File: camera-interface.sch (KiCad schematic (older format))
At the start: 44 parts, among them J8 WE_68715014522, U19 NTS0102GT, U20 NTS0102GT, U22 AP2114H-3_3TRG1

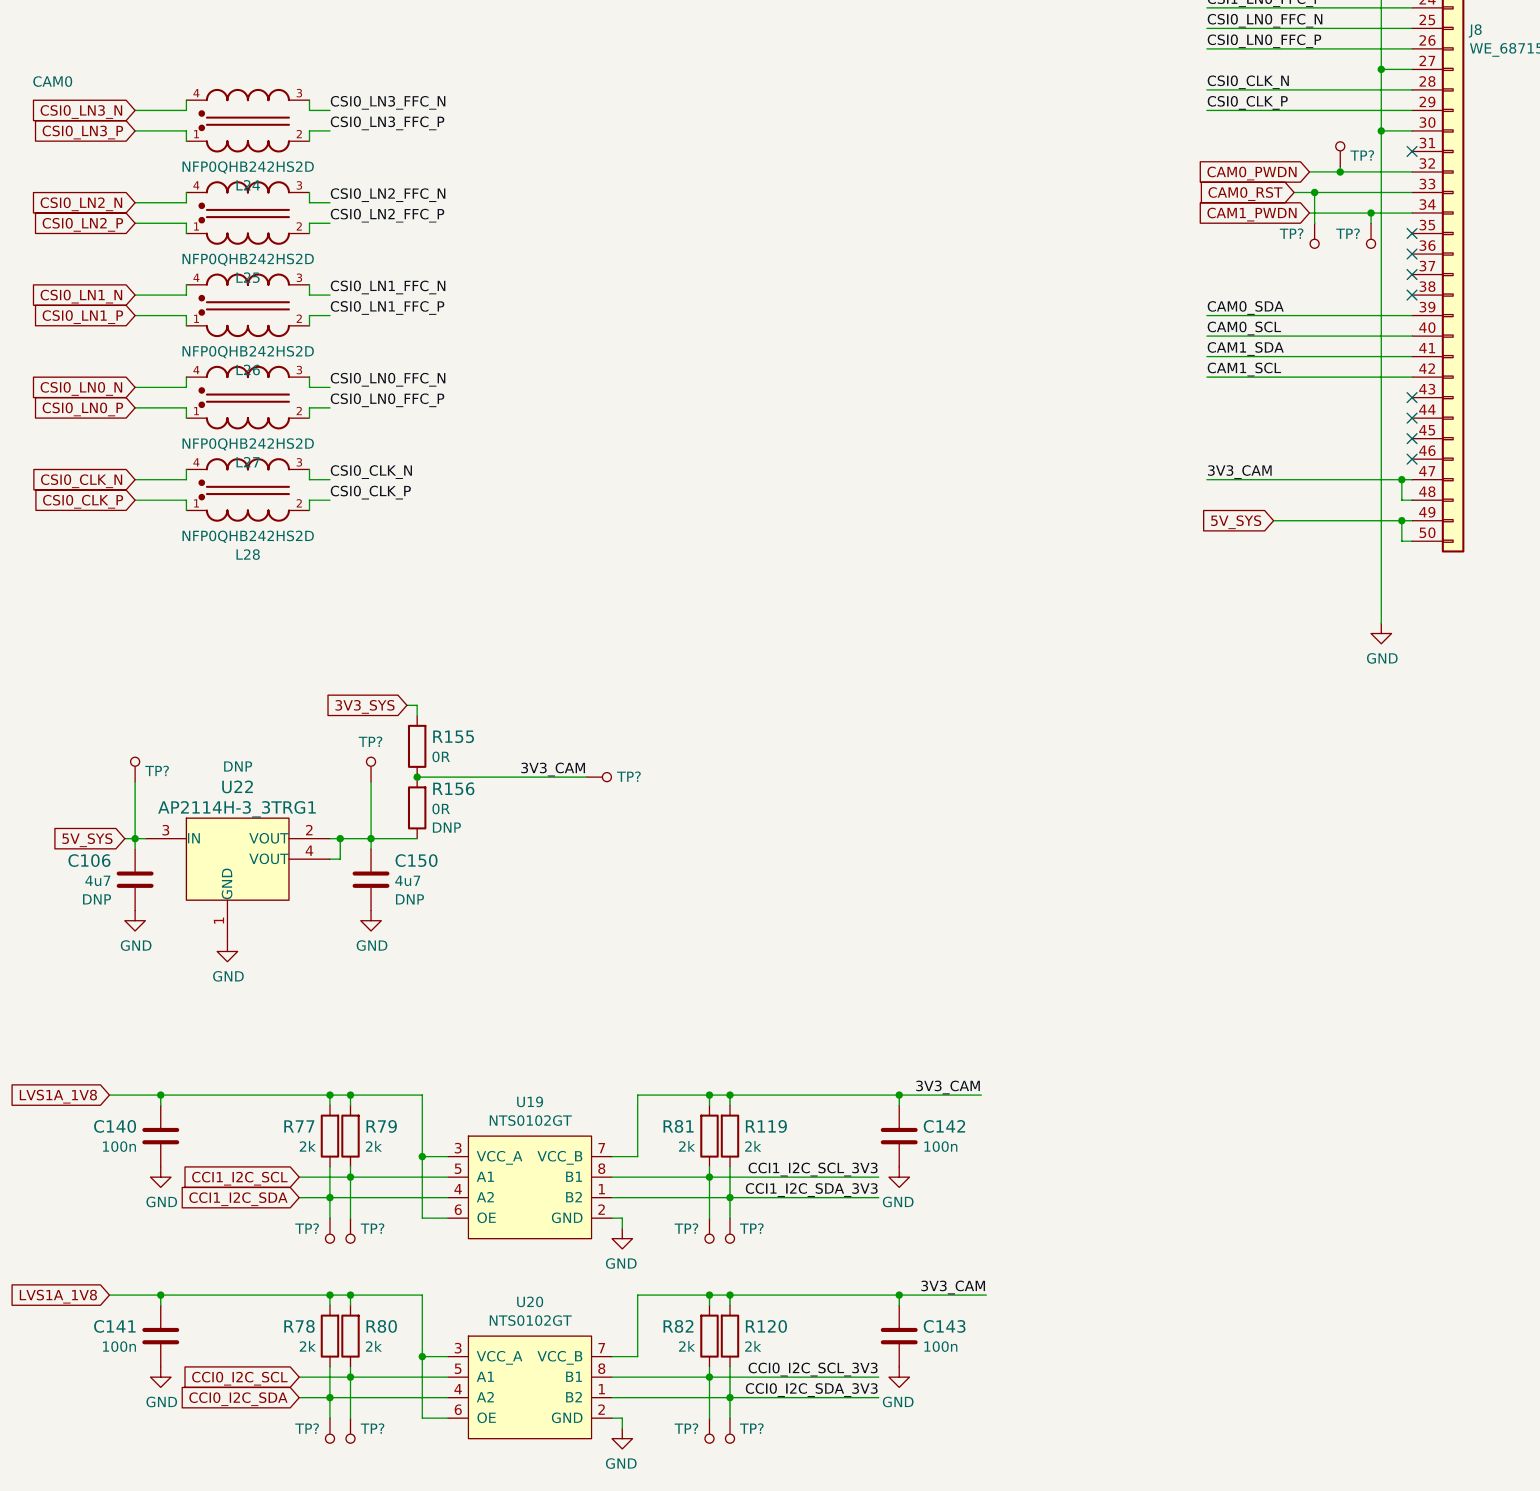
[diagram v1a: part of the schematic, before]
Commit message: Annotate test points, reimport 510R from global library
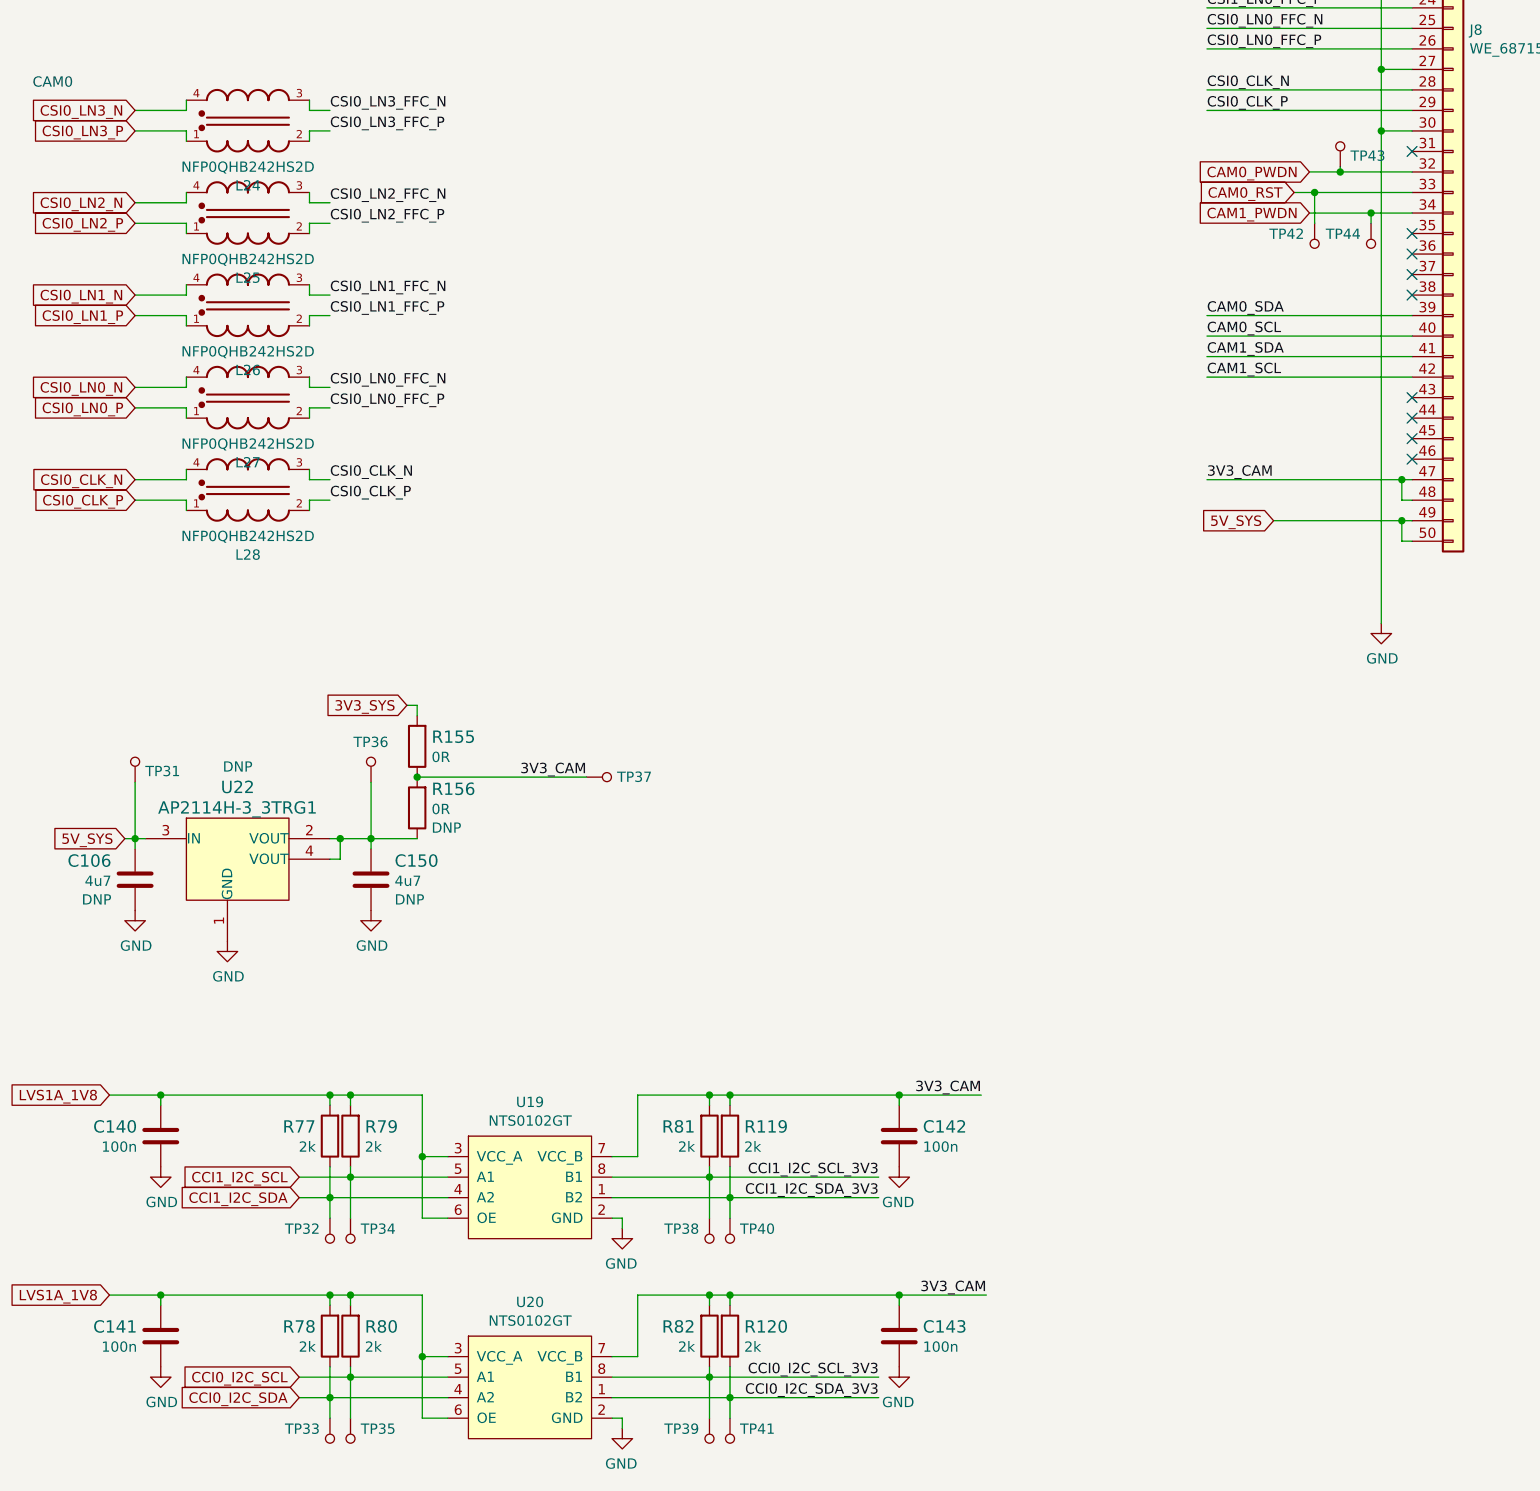
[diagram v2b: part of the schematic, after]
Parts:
- gave numbers to parts that had none: 14
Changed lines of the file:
@@
 AR Path="/618E716E/62E2A94F" Ref="TP?"  Part="1"
 AR Path="/6197686D/62E2A94F" Ref="TP?"  Part="1"
-F 0 "TP?" H 4076 9997 50  0000 R CNN
+AR Path="/61A60486/62E2A94F" Ref="TP40"  Part="1"
+F 0 "TP40" H 4076 9997 50  0000 R CNN
 F 1 "TP_SMD_0_75MM" H 4125 9850 50  0001 C CNN
 F 2 "antmicro-footprints:Testpoint_smd_0_75mm" H 4325 10150 60  0001 L CNN
@@
 AR Path="/618E716E/62E2A955" Ref="TP?"  Part="1"
 AR Path="/6197686D/62E2A955" Ref="TP?"  Part="1"
-F 0 "TP?" H 4075 9997 50  0000 L CNN
+AR Path="/61A60486/62E2A955" Ref="TP38"  Part="1"
+F 0 "TP38" H 4075 9997 50  0000 L CNN
 F 1 "TP_SMD_0_75MM" H 4025 9850 50  0001 C CNN
 F 2 "antmicro-footprints:Testpoint_smd_0_75mm" H 4225 10150 60  0001 L CNN
@@
 AR Path="/618E716E/62E363CD" Ref="TP?"  Part="1"
 AR Path="/6197686D/62E363CD" Ref="TP?"  Part="1"
-F 0 "TP?" H 4076 10972 50  0000 R CNN
+AR Path="/61A60486/62E363CD" Ref="TP41"  Part="1"
+F 0 "TP41" H 4076 10972 50  0000 R CNN
 F 1 "TP_SMD_0_75MM" H 4125 10825 50  0001 C CNN
 F 2 "antmicro-footprints:Testpoint_smd_0_75mm" H 4325 11125 60  0001 L CNN
@@
 AR Path="/618E716E/62E363D3" Ref="TP?"  Part="1"
 AR Path="/6197686D/62E363D3" Ref="TP?"  Part="1"
-F 0 "TP?" H 4075 10972 50  0000 L CNN
+AR Path="/61A60486/62E363D3" Ref="TP39"  Part="1"
+F 0 "TP39" H 4075 10972 50  0000 L CNN
 F 1 "TP_SMD_0_75MM" H 4025 10825 50  0001 C CNN
 F 2 "antmicro-footprints:Testpoint_smd_0_75mm" H 4225 11125 60  0001 L CNN
@@
 AR Path="/618E716E/62E41C82" Ref="TP?"  Part="1"
 AR Path="/6197686D/62E41C82" Ref="TP?"  Part="1"
-F 0 "TP?" H 2126 10972 50  0000 R CNN
+AR Path="/61A60486/62E41C82" Ref="TP33"  Part="1"
+F 0 "TP33" H 2126 10972 50  0000 R CNN
 F 1 "TP_SMD_0_75MM" H 2175 10825 50  0001 C CNN
 F 2 "antmicro-footprints:Testpoint_smd_0_75mm" H 2375 11125 60  0001 L CNN
@@
 AR Path="/618E716E/62E41C88" Ref="TP?"  Part="1"
 AR Path="/6197686D/62E41C88" Ref="TP?"  Part="1"
-F 0 "TP?" H 2325 10972 50  0000 L CNN
+AR Path="/61A60486/62E41C88" Ref="TP35"  Part="1"
+F 0 "TP35" H 2325 10972 50  0000 L CNN
 F 1 "TP_SMD_0_75MM" H 2275 10825 50  0001 C CNN
 F 2 "antmicro-footprints:Testpoint_smd_0_75mm" H 2475 11125 60  0001 L CNN
@@
 AR Path="/618E716E/62E4DB47" Ref="TP?"  Part="1"
 AR Path="/6197686D/62E4DB47" Ref="TP?"  Part="1"
-F 0 "TP?" H 2126 9997 50  0000 R CNN
+AR Path="/61A60486/62E4DB47" Ref="TP32"  Part="1"
+F 0 "TP32" H 2126 9997 50  0000 R CNN
 F 1 "TP_SMD_0_75MM" H 2175 9850 50  0001 C CNN
 F 2 "antmicro-footprints:Testpoint_smd_0_75mm" H 2375 10150 60  0001 L CNN
@@
 AR Path="/618E716E/62E4DB4D" Ref="TP?"  Part="1"
 AR Path="/6197686D/62E4DB4D" Ref="TP?"  Part="1"
-F 0 "TP?" H 2325 9997 50  0000 L CNN
+AR Path="/61A60486/62E4DB4D" Ref="TP34"  Part="1"
+F 0 "TP34" H 2325 9997 50  0000 L CNN
 F 1 "TP_SMD_0_75MM" H 2275 9850 50  0001 C CNN
 F 2 "antmicro-footprints:Testpoint_smd_0_75mm" H 2475 10150 60  0001 L CNN
@@
 AR Path="/618E716E/62E6257B" Ref="TP?"  Part="1"
 AR Path="/6197686D/62E6257B" Ref="TP?"  Part="1"
-AR Path="/61A60486/62E6257B" Ref="TP?"  Part="1"
-F 0 "TP?" H 1175 7672 50  0000 R CNN
+AR Path="/61A60486/62E6257B" Ref="TP31"  Part="1"
+F 0 "TP31" H 1175 7672 50  0000 R CNN
 F 1 "TP_SMD_0_75MM" H 1225 7525 50  0001 C CNN
 F 2 "antmicro-footprints:Testpoint_smd_0_75mm" H 1425 7825 60  0001 L CNN
@@
 AR Path="/618E716E/62E9438C" Ref="TP?"  Part="1"
 AR Path="/6197686D/62E9438C" Ref="TP?"  Part="1"
-AR Path="/61A60486/62E9438C" Ref="TP?"  Part="1"
-F 0 "TP?" H 2375 7530 50  0000 C CNN
+AR Path="/61A60486/62E9438C" Ref="TP36"  Part="1"
+F 0 "TP36" H 2375 7530 50  0000 C CNN
 F 1 "TP_SMD_0_75MM" H 2375 7525 50  0001 C CNN
 F 2 "antmicro-footprints:Testpoint_smd_0_75mm" H 2575 7825 60  0001 L CNN
@@
 AR Path="/618E716E/62EA24BE" Ref="TP?"  Part="1"
 AR Path="/6197686D/62EA24BE" Ref="TP?"  Part="1"
-AR Path="/61A60486/62EA24BE" Ref="TP?"  Part="1"
-F 0 "TP?" V 3525 7650 50  0000 R CNN
+AR Path="/61A60486/62EA24BE" Ref="TP37"  Part="1"
+F 0 "TP37" V 3525 7650 50  0000 R CNN
 F 1 "TP_SMD_0_75MM" H 3525 7600 50  0001 C CNN
 F 2 "antmicro-footprints:Testpoint_smd_0_75mm" H 3725 7900 60  0001 L CNN
@@
 AR Path="/618E716E/62EB9E73" Ref="TP?"  Part="1"
 AR Path="/6197686D/62EB9E73" Ref="TP?"  Part="1"
-AR Path="/61A60486/62EB9E73" Ref="TP?"  Part="1"
-F 0 "TP?" H 7050 4672 50  0000 R CNN
+AR Path="/61A60486/62EB9E73" Ref="TP43"  Part="1"
+F 0 "TP43" H 7050 4672 50  0000 R CNN
 F 1 "TP_SMD_0_75MM" H 7100 4525 50  0001 C CNN
 F 2 "antmicro-footprints:Testpoint_smd_0_75mm" H 7300 4825 60  0001 L CNN
@@
 AR Path="/618E716E/62EDF1A3" Ref="TP?"  Part="1"
 AR Path="/6197686D/62EDF1A3" Ref="TP?"  Part="1"
-AR Path="/61A60486/62EDF1A3" Ref="TP?"  Part="1"
-F 0 "TP?" H 6925 5147 50  0000 R CNN
+AR Path="/61A60486/62EDF1A3" Ref="TP42"  Part="1"
+F 0 "TP42" H 6925 5147 50  0000 R CNN
 F 1 "TP_SMD_0_75MM" H 6975 5000 50  0001 C CNN
 F 2 "antmicro-footprints:Testpoint_smd_0_75mm" H 7175 5300 60  0001 L CNN
@@
 AR Path="/618E716E/62EF7916" Ref="TP?"  Part="1"
 AR Path="/6197686D/62EF7916" Ref="TP?"  Part="1"
-AR Path="/61A60486/62EF7916" Ref="TP?"  Part="1"
-F 0 "TP?" H 7200 5147 50  0000 R CNN
+AR Path="/61A60486/62EF7916" Ref="TP44"  Part="1"
+F 0 "TP44" H 7200 5147 50  0000 R CNN
 F 1 "TP_SMD_0_75MM" H 7250 5000 50  0001 C CNN
 F 2 "antmicro-footprints:Testpoint_smd_0_75mm" H 7450 5300 60  0001 L CNN

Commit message: Loclib
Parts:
- TP31, TP32, TP33, TP34, TP35, TP36, TP37, TP38, TP39, TP40, TP41, TP42, TP43, TP44: footprint antmicro-footprints:Testpoint_smd_0_75mm -> sa800u-baseboard-hw-footprints:Testpoint_smd_0_75mm; symbol antmicroTestPoints:TP_SMD_0_75MM -> sa800u-baseboard-hw:TP_SMD_0_75MM
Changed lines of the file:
@@
 	7400 6250 7450 6250
 $Comp
-L antmicroTestPoints:TP_SMD_0_75MM TP?
+L sa800u-baseboard-hw:TP_SMD_0_75MM TP?
 U 1 1 62E2A94F
 P 4125 9950
@@
 F 0 "TP40" H 4076 9997 50  0000 R CNN
 F 1 "TP_SMD_0_75MM" H 4125 9850 50  0001 C CNN
-F 2 "antmicro-footprints:Testpoint_smd_0_75mm" H 4325 10150 60  0001 L CNN
+F 2 "sa800u-baseboard-hw-footprints:Testpoint_smd_0_75mm" H 4325 10150 60  0001 L CNN
 F 3 "" H 4325 10250 60  0001 L CNN
 	1    4125 9950
@@
 $EndComp
 $Comp
-L antmicroTestPoints:TP_SMD_0_75MM TP?
+L sa800u-baseboard-hw:TP_SMD_0_75MM TP?
 U 1 1 62E2A955
 P 4025 9950
@@
 F 0 "TP38" H 4075 9997 50  0000 L CNN
 F 1 "TP_SMD_0_75MM" H 4025 9850 50  0001 C CNN
-F 2 "antmicro-footprints:Testpoint_smd_0_75mm" H 4225 10150 60  0001 L CNN
+F 2 "sa800u-baseboard-hw-footprints:Testpoint_smd_0_75mm" H 4225 10150 60  0001 L CNN
 F 3 "" H 4225 10250 60  0001 L CNN
 	1    4025 9950
@@
 	4025 9850 4025 9650
 $Comp
-L antmicroTestPoints:TP_SMD_0_75MM TP?
+L sa800u-baseboard-hw:TP_SMD_0_75MM TP?
 U 1 1 62E363CD
 P 4125 10925
@@
 F 0 "TP41" H 4076 10972 50  0000 R CNN
 F 1 "TP_SMD_0_75MM" H 4125 10825 50  0001 C CNN
-F 2 "antmicro-footprints:Testpoint_smd_0_75mm" H 4325 11125 60  0001 L CNN
+F 2 "sa800u-baseboard-hw-footprints:Testpoint_smd_0_75mm" H 4325 11125 60  0001 L CNN
 F 3 "" H 4325 11225 60  0001 L CNN
 	1    4125 10925
@@
 $EndComp
 $Comp
-L antmicroTestPoints:TP_SMD_0_75MM TP?
+L sa800u-baseboard-hw:TP_SMD_0_75MM TP?
 U 1 1 62E363D3
 P 4025 10925
@@
 F 0 "TP39" H 4075 10972 50  0000 L CNN
 F 1 "TP_SMD_0_75MM" H 4025 10825 50  0001 C CNN
-F 2 "antmicro-footprints:Testpoint_smd_0_75mm" H 4225 11125 60  0001 L CNN
+F 2 "sa800u-baseboard-hw-footprints:Testpoint_smd_0_75mm" H 4225 11125 60  0001 L CNN
 F 3 "" H 4225 11225 60  0001 L CNN
 	1    4025 10925
@@
 	4025 10825 4025 10625
 $Comp
-L antmicroTestPoints:TP_SMD_0_75MM TP?
+L sa800u-baseboard-hw:TP_SMD_0_75MM TP?
 U 1 1 62E41C82
 P 2175 10925
@@
 F 0 "TP33" H 2126 10972 50  0000 R CNN
 F 1 "TP_SMD_0_75MM" H 2175 10825 50  0001 C CNN
-F 2 "antmicro-footprints:Testpoint_smd_0_75mm" H 2375 11125 60  0001 L CNN
+F 2 "sa800u-baseboard-hw-footprints:Testpoint_smd_0_75mm" H 2375 11125 60  0001 L CNN
 F 3 "" H 2375 11225 60  0001 L CNN
 	1    2175 10925
@@
 $EndComp
 $Comp
-L antmicroTestPoints:TP_SMD_0_75MM TP?
+L sa800u-baseboard-hw:TP_SMD_0_75MM TP?
 U 1 1 62E41C88
 P 2275 10925
@@
 F 0 "TP35" H 2325 10972 50  0000 L CNN
 F 1 "TP_SMD_0_75MM" H 2275 10825 50  0001 C CNN
-F 2 "antmicro-footprints:Testpoint_smd_0_75mm" H 2475 11125 60  0001 L CNN
+F 2 "sa800u-baseboard-hw-footprints:Testpoint_smd_0_75mm" H 2475 11125 60  0001 L CNN
 F 3 "" H 2475 11225 60  0001 L CNN
 	1    2275 10925
@@
 	2275 10825 2275 10625
 $Comp
-L antmicroTestPoints:TP_SMD_0_75MM TP?
+L sa800u-baseboard-hw:TP_SMD_0_75MM TP?
 U 1 1 62E4DB47
 P 2175 9950
@@
 F 0 "TP32" H 2126 9997 50  0000 R CNN
 F 1 "TP_SMD_0_75MM" H 2175 9850 50  0001 C CNN
-F 2 "antmicro-footprints:Testpoint_smd_0_75mm" H 2375 10150 60  0001 L CNN
+F 2 "sa800u-baseboard-hw-footprints:Testpoint_smd_0_75mm" H 2375 10150 60  0001 L CNN
 F 3 "" H 2375 10250 60  0001 L CNN
 	1    2175 9950
@@
 $EndComp
 $Comp
-L antmicroTestPoints:TP_SMD_0_75MM TP?
+L sa800u-baseboard-hw:TP_SMD_0_75MM TP?
 U 1 1 62E4DB4D
 P 2275 9950
@@
 F 0 "TP34" H 2325 9997 50  0000 L CNN
 F 1 "TP_SMD_0_75MM" H 2275 9850 50  0001 C CNN
-F 2 "antmicro-footprints:Testpoint_smd_0_75mm" H 2475 10150 60  0001 L CNN
+F 2 "sa800u-baseboard-hw-footprints:Testpoint_smd_0_75mm" H 2475 10150 60  0001 L CNN
 F 3 "" H 2475 10250 60  0001 L CNN
 	1    2275 9950
@@
 	2275 9850 2275 9650
 $Comp
-L antmicroTestPoints:TP_SMD_0_75MM TP?
+L sa800u-baseboard-hw:TP_SMD_0_75MM TP?
 U 1 1 62E6257B
 P 1225 7625
@@
 F 0 "TP31" H 1175 7672 50  0000 R CNN
 F 1 "TP_SMD_0_75MM" H 1225 7525 50  0001 C CNN
-F 2 "antmicro-footprints:Testpoint_smd_0_75mm" H 1425 7825 60  0001 L CNN
+F 2 "sa800u-baseboard-hw-footprints:Testpoint_smd_0_75mm" H 1425 7825 60  0001 L CNN
 F 3 "" H 1425 7925 60  0001 L CNN
 	1    1225 7625
@@
 	1225 7725 1225 8000
 $Comp
-L antmicroTestPoints:TP_SMD_0_75MM TP?
+L sa800u-baseboard-hw:TP_SMD_0_75MM TP?
 U 1 1 62E9438C
 P 2375 7625
@@
 F 0 "TP36" H 2375 7530 50  0000 C CNN
 F 1 "TP_SMD_0_75MM" H 2375 7525 50  0001 C CNN
-F 2 "antmicro-footprints:Testpoint_smd_0_75mm" H 2575 7825 60  0001 L CNN
+F 2 "sa800u-baseboard-hw-footprints:Testpoint_smd_0_75mm" H 2575 7825 60  0001 L CNN
 F 3 "" H 2575 7925 60  0001 L CNN
 	1    2375 7625
@@
 	2375 7725 2375 8000
 $Comp
-L antmicroTestPoints:TP_SMD_0_75MM TP?
+L sa800u-baseboard-hw:TP_SMD_0_75MM TP?
 U 1 1 62EA24BE
 P 3525 7700
@@
 F 0 "TP37" V 3525 7650 50  0000 R CNN
 F 1 "TP_SMD_0_75MM" H 3525 7600 50  0001 C CNN
-F 2 "antmicro-footprints:Testpoint_smd_0_75mm" H 3725 7900 60  0001 L CNN
+F 2 "sa800u-baseboard-hw-footprints:Testpoint_smd_0_75mm" H 3725 7900 60  0001 L CNN
 F 3 "" H 3725 8000 60  0001 L CNN
 	1    3525 7700
@@
 $EndComp
 $Comp
-L antmicroTestPoints:TP_SMD_0_75MM TP?
+L sa800u-baseboard-hw:TP_SMD_0_75MM TP?
 U 1 1 62EB9E73
 P 7100 4625
@@
 F 0 "TP43" H 7050 4672 50  0000 R CNN
 F 1 "TP_SMD_0_75MM" H 7100 4525 50  0001 C CNN
-F 2 "antmicro-footprints:Testpoint_smd_0_75mm" H 7300 4825 60  0001 L CNN
+F 2 "sa800u-baseboard-hw-footprints:Testpoint_smd_0_75mm" H 7300 4825 60  0001 L CNN
 F 3 "" H 7300 4925 60  0001 L CNN
 	1    7100 4625
@@
 	7100 4750 6950 4750
 $Comp
-L antmicroTestPoints:TP_SMD_0_75MM TP?
+L sa800u-baseboard-hw:TP_SMD_0_75MM TP?
 U 1 1 62EDF1A3
 P 6975 5100
@@
 F 0 "TP42" H 6925 5147 50  0000 R CNN
 F 1 "TP_SMD_0_75MM" H 6975 5000 50  0001 C CNN
-F 2 "antmicro-footprints:Testpoint_smd_0_75mm" H 7175 5300 60  0001 L CNN
+F 2 "sa800u-baseboard-hw-footprints:Testpoint_smd_0_75mm" H 7175 5300 60  0001 L CNN
 F 3 "" H 7175 5400 60  0001 L CNN
 	1    6975 5100
@@
 	6975 4850 6875 4850
 $Comp
-L antmicroTestPoints:TP_SMD_0_75MM TP?
+L sa800u-baseboard-hw:TP_SMD_0_75MM TP?
 U 1 1 62EF7916
 P 7250 5100
@@
 F 0 "TP44" H 7200 5147 50  0000 R CNN
 F 1 "TP_SMD_0_75MM" H 7250 5000 50  0001 C CNN
-F 2 "antmicro-footprints:Testpoint_smd_0_75mm" H 7450 5300 60  0001 L CNN
+F 2 "sa800u-baseboard-hw-footprints:Testpoint_smd_0_75mm" H 7450 5300 60  0001 L CNN
 F 3 "" H 7450 5400 60  0001 L CNN
 	1    7250 5100
